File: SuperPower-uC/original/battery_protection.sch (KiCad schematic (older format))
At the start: 11 parts, among them J1 JST_PH_S2B_thru, Q1 DMN2019UTS, U1 AP9101CK6-AYTRG1

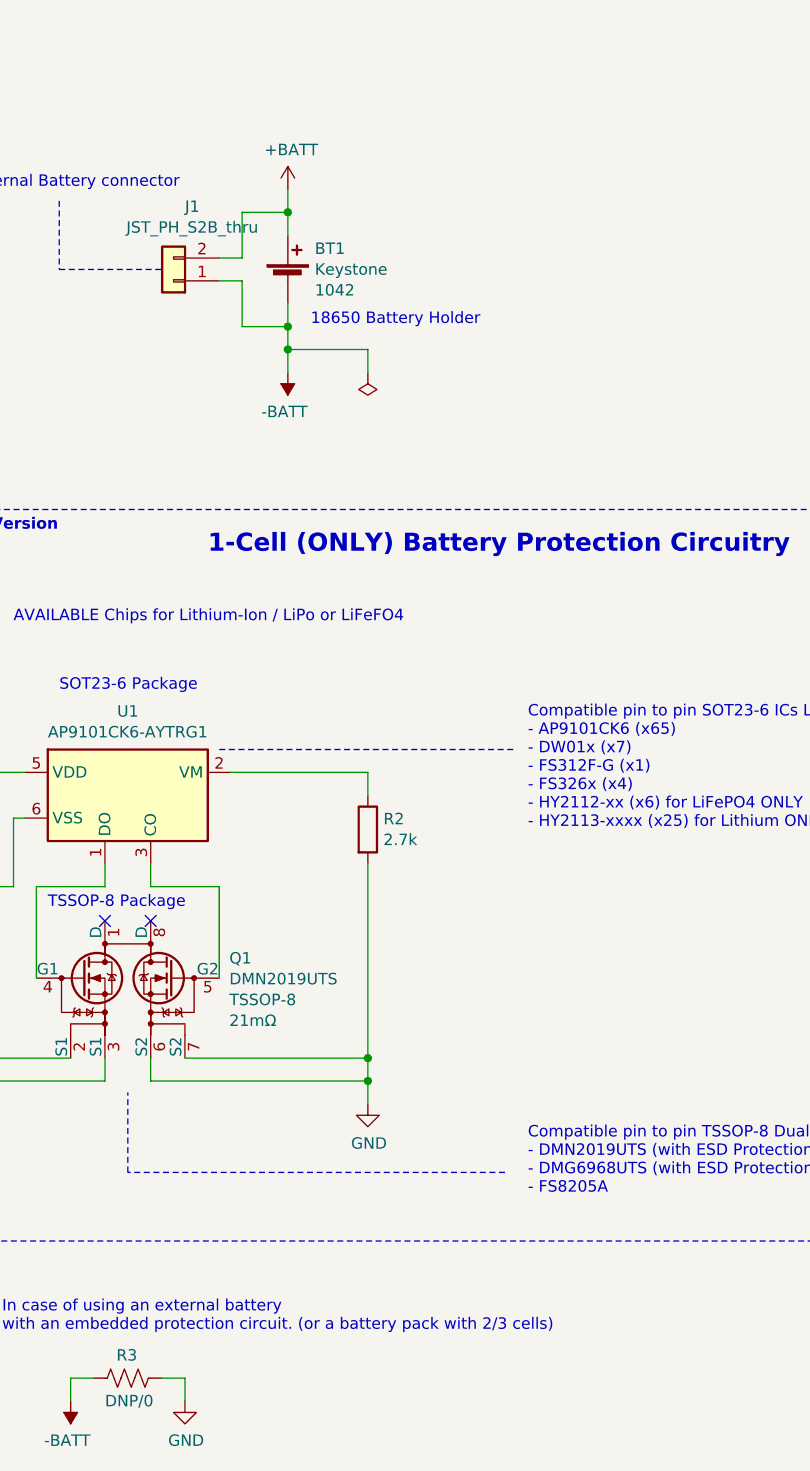
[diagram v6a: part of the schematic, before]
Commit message: Update "Charger Sheet" components
IC, Capacitors, Inductor and Connectors + Misc. Text
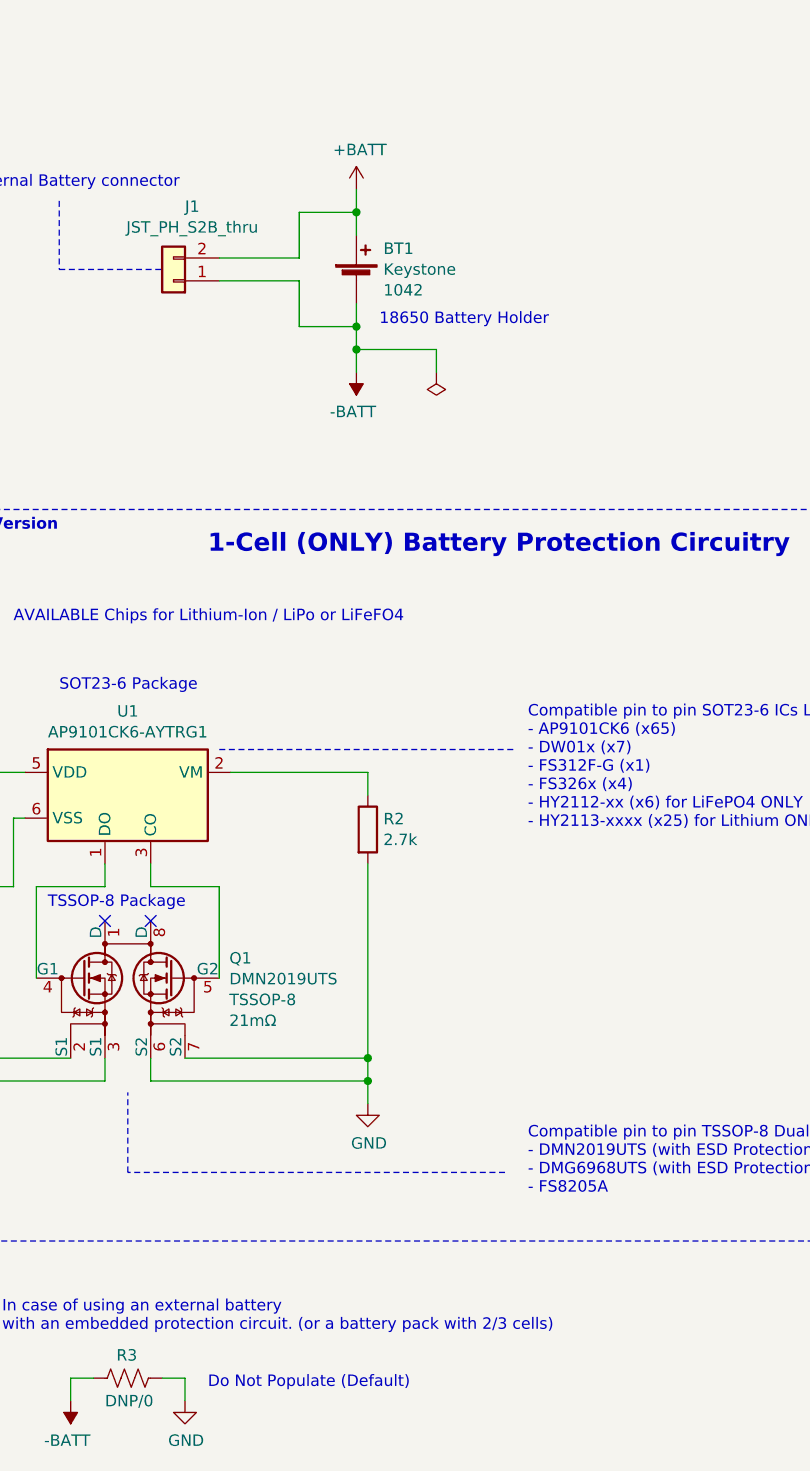
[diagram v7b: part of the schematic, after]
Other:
- note added: "Do Not Populate (Default)"
- moved on the sheet: BT1
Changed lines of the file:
@@
 L power:-BATT #PWR04
 U 1 1 5F7A20F6
-P 3500 2100
-F 0 "#PWR04" H 3500 1950 50  0001 C CNN
-F 1 "-BATT" H 3515 2273 50  0000 C CNN
-F 2 "" H 3500 2100 50  0001 C CNN
-F 3 "" H 3500 2100 50  0001 C CNN
-	1    3500 2100
+P 3800 2100
+F 0 "#PWR04" H 3800 1950 50  0001 C CNN
+F 1 "-BATT" H 3815 2273 50  0000 C CNN
+F 2 "" H 3800 2100 50  0001 C CNN
+F 3 "" H 3800 2100 50  0001 C CNN
+	1    3800 2100
 	-1   0    0    1
 $EndComp
@@
 L power:+BATT #PWR03
 U 1 1 5F7A2546
-P 3500 1300
-F 0 "#PWR03" H 3500 1150 50  0001 C CNN
-F 1 "+BATT" H 3515 1473 50  0000 C CNN
-F 2 "" H 3500 1300 50  0001 C CNN
-F 3 "" H 3500 1300 50  0001 C CNN
-	1    3500 1300
-	1    0    0    -1
-$EndComp
-Wire Wire Line
-	3500 1500 3500 1400
-Wire Wire Line
-	3500 1800 3500 1900
-Wire Wire Line
-	3300 1700 3300 1900
-Wire Wire Line
-	3300 1900 3500 1900
-Wire Wire Line
-	3500 1900 3500 2000
-Wire Wire Line
-	3300 1600 3300 1400
-Wire Wire Line
-	3300 1400 3500 1400
-Connection ~ 3500 1400
-Wire Wire Line
-	3500 1400 3500 1300
+P 3800 1300
+F 0 "#PWR03" H 3800 1150 50  0001 C CNN
+F 1 "+BATT" H 3815 1473 50  0000 C CNN
+F 2 "" H 3800 1300 50  0001 C CNN
+F 3 "" H 3800 1300 50  0001 C CNN
+	1    3800 1300
+	1    0    0    -1
+$EndComp
+Wire Wire Line
+	3800 1500 3800 1400
+Wire Wire Line
+	3800 1800 3800 1900
+Wire Wire Line
+	3550 1700 3550 1900
+Wire Wire Line
+	3550 1900 3800 1900
+Wire Wire Line
+	3800 1900 3800 2000
+Wire Wire Line
+	3550 1600 3550 1400
+Wire Wire Line
+	3550 1400 3800 1400
+Connection ~ 3800 1400
+Wire Wire Line
+	3800 1400 3800 1300
 Text Notes 8150 2450 0    50   ~ 0
 Chinese Chip price range from LCSC (10/2020) :\n$0.075-0.115 @qt=10\n$0.054-0.087 @qt=100
@@
 L power:PWR_FLAG #FLG03
 U 1 1 5F8B1179
-P 3850 2100
-F 0 "#FLG03" H 3850 2175 50  0001 C CNN
-F 1 "PWR_FLAG" H 3850 2273 50  0001 C CNN
-F 2 "" H 3850 2100 50  0001 C CNN
-F 3 "~" H 3850 2100 50  0001 C CNN
-	1    3850 2100
+P 4150 2100
+F 0 "#FLG03" H 4150 2175 50  0001 C CNN
+F 1 "PWR_FLAG" H 4150 2273 50  0001 C CNN
+F 2 "" H 4150 2100 50  0001 C CNN
+F 3 "~" H 4150 2100 50  0001 C CNN
+	1    4150 2100
 	-1   0    0    1
 $EndComp
 Wire Wire Line
-	3850 2100 3850 2000
-Wire Wire Line
-	3850 2000 3500 2000
-Connection ~ 3500 2000
-Wire Wire Line
-	3500 2000 3500 2100
+	4150 2100 4150 2000
+Wire Wire Line
+	4150 2000 3800 2000
+Connection ~ 3800 2000
+Wire Wire Line
+	3800 2000 3800 2100
 Connection ~ 1900 3350
 Wire Wire Line
@@
 Connection ~ 3850 5200
 Wire Wire Line
-	3200 1600 3300 1600
-Wire Wire Line
-	3300 1700 3200 1700
-Connection ~ 3500 1900
+	3200 1600 3550 1600
+Wire Wire Line
+	3550 1700 3200 1700
+Connection ~ 3800 1900
 Text Notes 2100 1300 0    50   ~ 0
 External Battery connector
@@
 Wire Notes Line
 	1250 2700 1250 5900
-Text Notes 3600 1900 0    50   ~ 0
+Text Notes 3900 1900 0    50   ~ 0
 18650 Battery Holder
 Wire Notes Line
@@
 L battery_cell_holder_18650_smt_1042:Battery_Cell_Holder_18650_SMT_1042 BT1
 U 1 1 5FD97812
-P 3500 1700
-F 0 "BT1" H 3618 1841 50  0000 L CNN
-F 1 "Battery_Cell_Holder_18650_SMT_1042" H 3600 1700 50  0001 L CNN
-F 2 "Battery:BatteryHolder_Keystone_1042_1x18650" V 3500 1760 50  0001 C CNN
-F 3 "https://www.keyelco.com/product-pdf.cfm?p=918" V 3500 1760 50  0001 C CNN
-F 4 "Keystone" H 3618 1750 50  0000 L CNN "Mfr_name"
-F 5 "1042" H 3618 1659 50  0000 L CNN "Mfr_no"
-F 6 "https://octopart.com/1042-keystone-19977746?r=sp#PriceAndStock" H 3500 1700 50  0001 C CNN "Octopart_link"
-F 7 "https://fr.farnell.com/keystone/1042p/battery-holder-18650-smd/dp/2674338?ost=keystone+1042" H 3500 1700 50  0001 C CNN "Farnell_link"
-F 8 "?" H 3500 1700 50  0001 C CNN "Farnell_ref"
-F 9 "2020-11-29" H 3500 1700 50  0001 C CNN "Farnell_check_date"
-F 10 "2,94 €" H 3500 1700 50  0001 C CNN "Farnell_price_qt=1"
-F 11 "2,65 €" H 3500 1700 50  0001 C CNN "Farnell_price_qt=10"
-F 12 "2,26 €" H 3500 1700 50  0001 C CNN "Farnell_price_qt=100"
-F 13 "1,62 €" H 3500 1700 50  0001 C CNN "Farnell_price_qt=1000"
-F 14 "Available from 2021-01-16" H 3500 1700 50  0001 C CNN "Farnell_stock"
-F 15 "-" H 3500 1700 50  0001 C CNN "LCSC_link"
-F 16 "-" H 3500 1700 50  0001 C CNN "LCSC_ref"
-F 17 "2020-11-29" H 3500 1700 50  0001 C CNN "LCSC_check_date"
-F 18 "-" H 3500 1700 50  0001 C CNN "LCSC_price_qt=1"
-F 19 "-" H 3500 1700 50  0001 C CNN "LCSC_price_qt=10"
-F 20 "-" H 3500 1700 50  0001 C CNN "LCSC_price_qt=100"
-F 21 "-" H 3500 1700 50  0001 C CNN "LCSC_price_qt=1000"
-F 22 "-" H 3500 1700 50  0001 C CNN "LCSC_stock"
-F 23 "https://eu.mouser.com/ProductDetail/Keystone-Electronics/1042?qs=%2F7TOpeL5Mz4qPdWi9tuLKw%3D%3D" H 3500 1700 50  0001 C CNN "Mouser_link"
-F 24 "?" H 3500 1700 50  0001 C CNN "Mouser_ref"
-F 25 "2020-11-29" H 3500 1700 50  0001 C CNN "Mouser_check_date"
-F 26 "$3.62" H 3500 1700 50  0001 C CNN "Mouser_price_qt=1"
-F 27 "-" H 3500 1700 50  0001 C CNN "Mouser_price_qt=10"
-F 28 "$3.13" H 3500 1700 50  0001 C CNN "Mouser_price_qt=100"
-F 29 "$2.36" H 3500 1700 50  0001 C CNN "Mouser_price_qt=1000"
-F 30 "3,942" H 3500 1700 50  0001 C CNN "Mouser_stock"
-F 31 "-" H 3500 1700 50  0001 C CNN "RS_link"
-F 32 "-" H 3500 1700 50  0001 C CNN "RS_ref"
-F 33 "2020-11-29" H 3500 1700 50  0001 C CNN "RS_check_date"
-F 34 "-" H 3500 1700 50  0001 C CNN "RS_price_qt=1"
-F 35 "-" H 3500 1700 50  0001 C CNN "RS_price_qt=10"
-F 36 "-" H 3500 1700 50  0001 C CNN "RS_price_qt=100"
-F 37 "-" H 3500 1700 50  0001 C CNN "RS_price_qt=1000"
-F 38 "-" H 3500 1700 50  0001 C CNN "RS_stock"
-F 39 "TO_CHECK" H 3500 1700 50  0001 C CNN "Status"
-F 40 "1.01" H 3500 1700 50  0001 C CNN "Release_version"
-F 41 "2020-12-12" H 3500 1700 50  0001 C CNN "Release_date"
-F 42 "ManWithNoName" H 3500 1700 50  0001 C CNN "Designer"
-	1    3500 1700
+P 3800 1700
+F 0 "BT1" H 3918 1841 50  0000 L CNN
+F 1 "Battery_Cell_Holder_18650_SMT_1042" H 3900 1700 50  0001 L CNN
+F 2 "Battery:BatteryHolder_Keystone_1042_1x18650" V 3800 1760 50  0001 C CNN
+F 3 "https://www.keyelco.com/product-pdf.cfm?p=918" V 3800 1760 50  0001 C CNN
+F 4 "Keystone" H 3918 1750 50  0000 L CNN "Mfr_name"
+F 5 "1042" H 3918 1659 50  0000 L CNN "Mfr_no"
+F 6 "https://octopart.com/1042-keystone-19977746?r=sp#PriceAndStock" H 3800 1700 50  0001 C CNN "Octopart_link"
+F 7 "https://fr.farnell.com/keystone/1042p/battery-holder-18650-smd/dp/2674338?ost=keystone+1042" H 3800 1700 50  0001 C CNN "Farnell_link"
+F 8 "?" H 3800 1700 50  0001 C CNN "Farnell_ref"
+F 9 "2020-11-29" H 3800 1700 50  0001 C CNN "Farnell_check_date"
+F 10 "2,94 €" H 3800 1700 50  0001 C CNN "Farnell_price_qt=1"
+F 11 "2,65 €" H 3800 1700 50  0001 C CNN "Farnell_price_qt=10"
+F 12 "2,26 €" H 3800 1700 50  0001 C CNN "Farnell_price_qt=100"
+F 13 "1,62 €" H 3800 1700 50  0001 C CNN "Farnell_price_qt=1000"
+F 14 "Available from 2021-01-16" H 3800 1700 50  0001 C CNN "Farnell_stock"
+F 15 "-" H 3800 1700 50  0001 C CNN "LCSC_link"
+F 16 "-" H 3800 1700 50  0001 C CNN "LCSC_ref"
+F 17 "2020-11-29" H 3800 1700 50  0001 C CNN "LCSC_check_date"
+F 18 "-" H 3800 1700 50  0001 C CNN "LCSC_price_qt=1"
+F 19 "-" H 3800 1700 50  0001 C CNN "LCSC_price_qt=10"
+F 20 "-" H 3800 1700 50  0001 C CNN "LCSC_price_qt=100"
+F 21 "-" H 3800 1700 50  0001 C CNN "LCSC_price_qt=1000"
+F 22 "-" H 3800 1700 50  0001 C CNN "LCSC_stock"
+F 23 "https://eu.mouser.com/ProductDetail/Keystone-Electronics/1042?qs=%2F7TOpeL5Mz4qPdWi9tuLKw%3D%3D" H 3800 1700 50  0001 C CNN "Mouser_link"
+F 24 "?" H 3800 1700 50  0001 C CNN "Mouser_ref"
+F 25 "2020-11-29" H 3800 1700 50  0001 C CNN "Mouser_check_date"
+F 26 "$3.62" H 3800 1700 50  0001 C CNN "Mouser_price_qt=1"
+F 27 "-" H 3800 1700 50  0001 C CNN "Mouser_price_qt=10"
+F 28 "$3.13" H 3800 1700 50  0001 C CNN "Mouser_price_qt=100"
+F 29 "$2.36" H 3800 1700 50  0001 C CNN "Mouser_price_qt=1000"
+F 30 "3,942" H 3800 1700 50  0001 C CNN "Mouser_stock"
+F 31 "-" H 3800 1700 50  0001 C CNN "RS_link"
+F 32 "-" H 3800 1700 50  0001 C CNN "RS_ref"
+F 33 "2020-11-29" H 3800 1700 50  0001 C CNN "RS_check_date"
+F 34 "-" H 3800 1700 50  0001 C CNN "RS_price_qt=1"
+F 35 "-" H 3800 1700 50  0001 C CNN "RS_price_qt=10"
+F 36 "-" H 3800 1700 50  0001 C CNN "RS_price_qt=100"
+F 37 "-" H 3800 1700 50  0001 C CNN "RS_price_qt=1000"
+F 38 "-" H 3800 1700 50  0001 C CNN "RS_stock"
+F 39 "TO_CHECK" H 3800 1700 50  0001 C CNN "Status"
+F 40 "1.01" H 3800 1700 50  0001 C CNN "Release_version"
+F 41 "2020-12-12" H 3800 1700 50  0001 C CNN "Release_date"
+F 42 "ManWithNoName" H 3800 1700 50  0001 C CNN "Designer"
+	1    3800 1700
 	1    0    0    -1
 $EndComp
@@
 	-1   0    0    1
 $EndComp
+Text Notes 3150 6550 0    50   ~ 0
+Do Not Populate (Default)
 $EndSCHEMATC

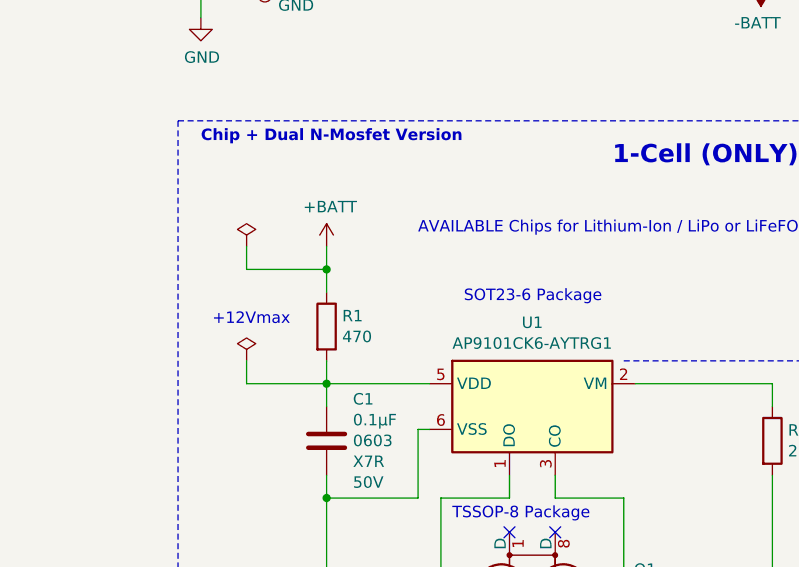
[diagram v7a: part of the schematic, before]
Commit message: Add / Update Test on the Main Sheet
+ Misc. Text
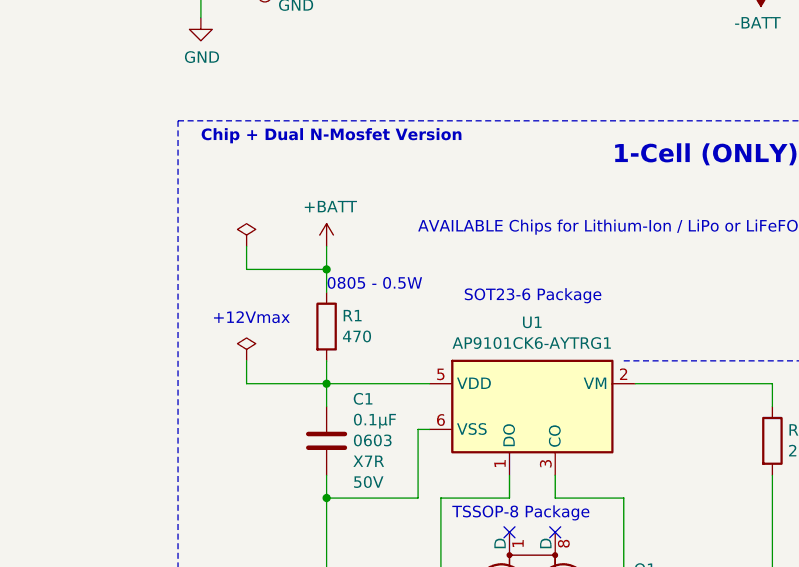
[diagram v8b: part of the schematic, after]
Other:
- note added: "0805 - 0.5W"
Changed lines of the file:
@@
 Text Notes 3150 6550 0    50   ~ 0
 Do Not Populate (Default)
+Text Notes 1900 3450 0    50   ~ 0
+0805 - 0.5W
 $EndSCHEMATC
